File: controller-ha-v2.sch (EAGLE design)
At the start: 138 parts, among them U1 DS1307, U2 ARDUINO-MEGAPRO-5V, U3 ARDUINO-MEGAFULL

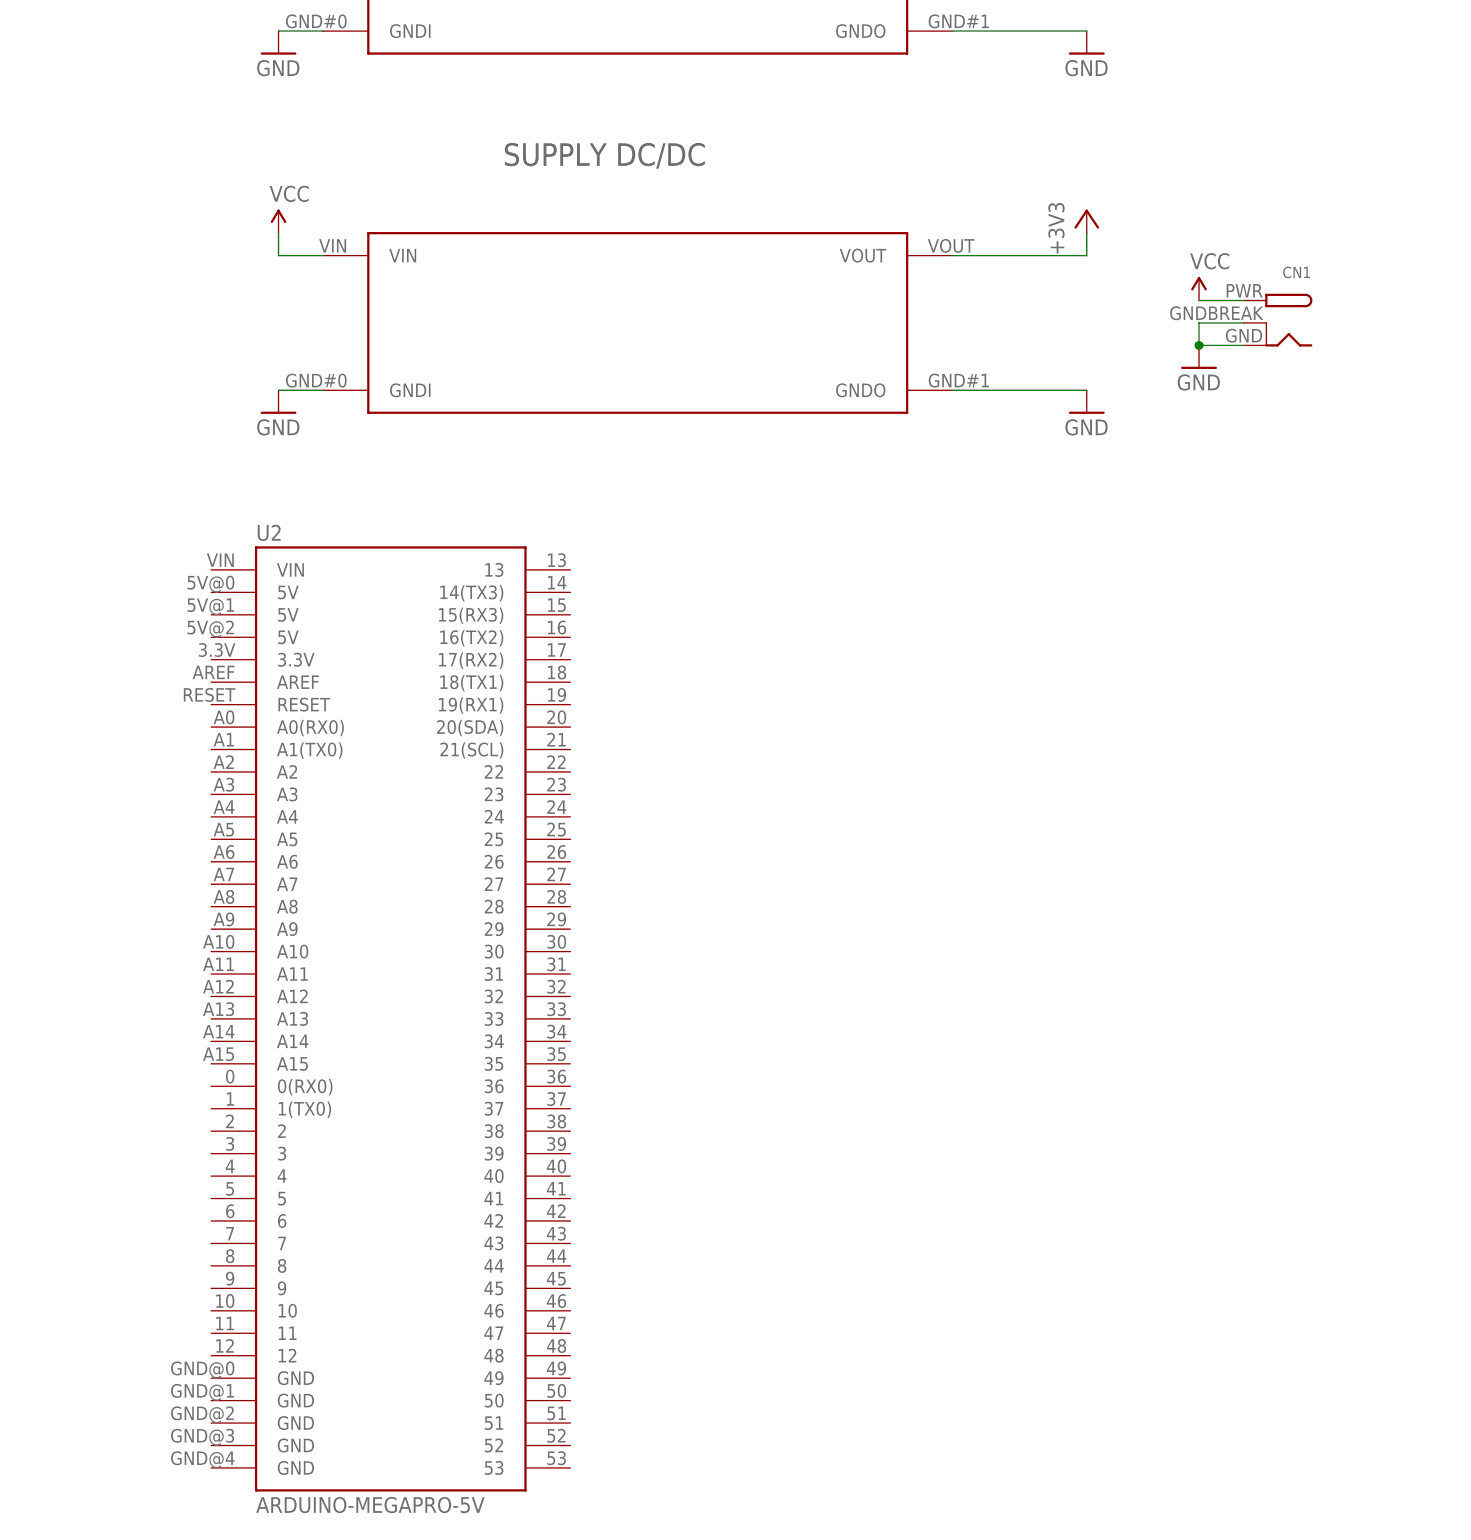
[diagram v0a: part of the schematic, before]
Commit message: Update to ver2
Added : Capacitors, DC/DC, DC input jack; Re-routed (fixed
too-close-through holes) + 9V DC and VCC clearence
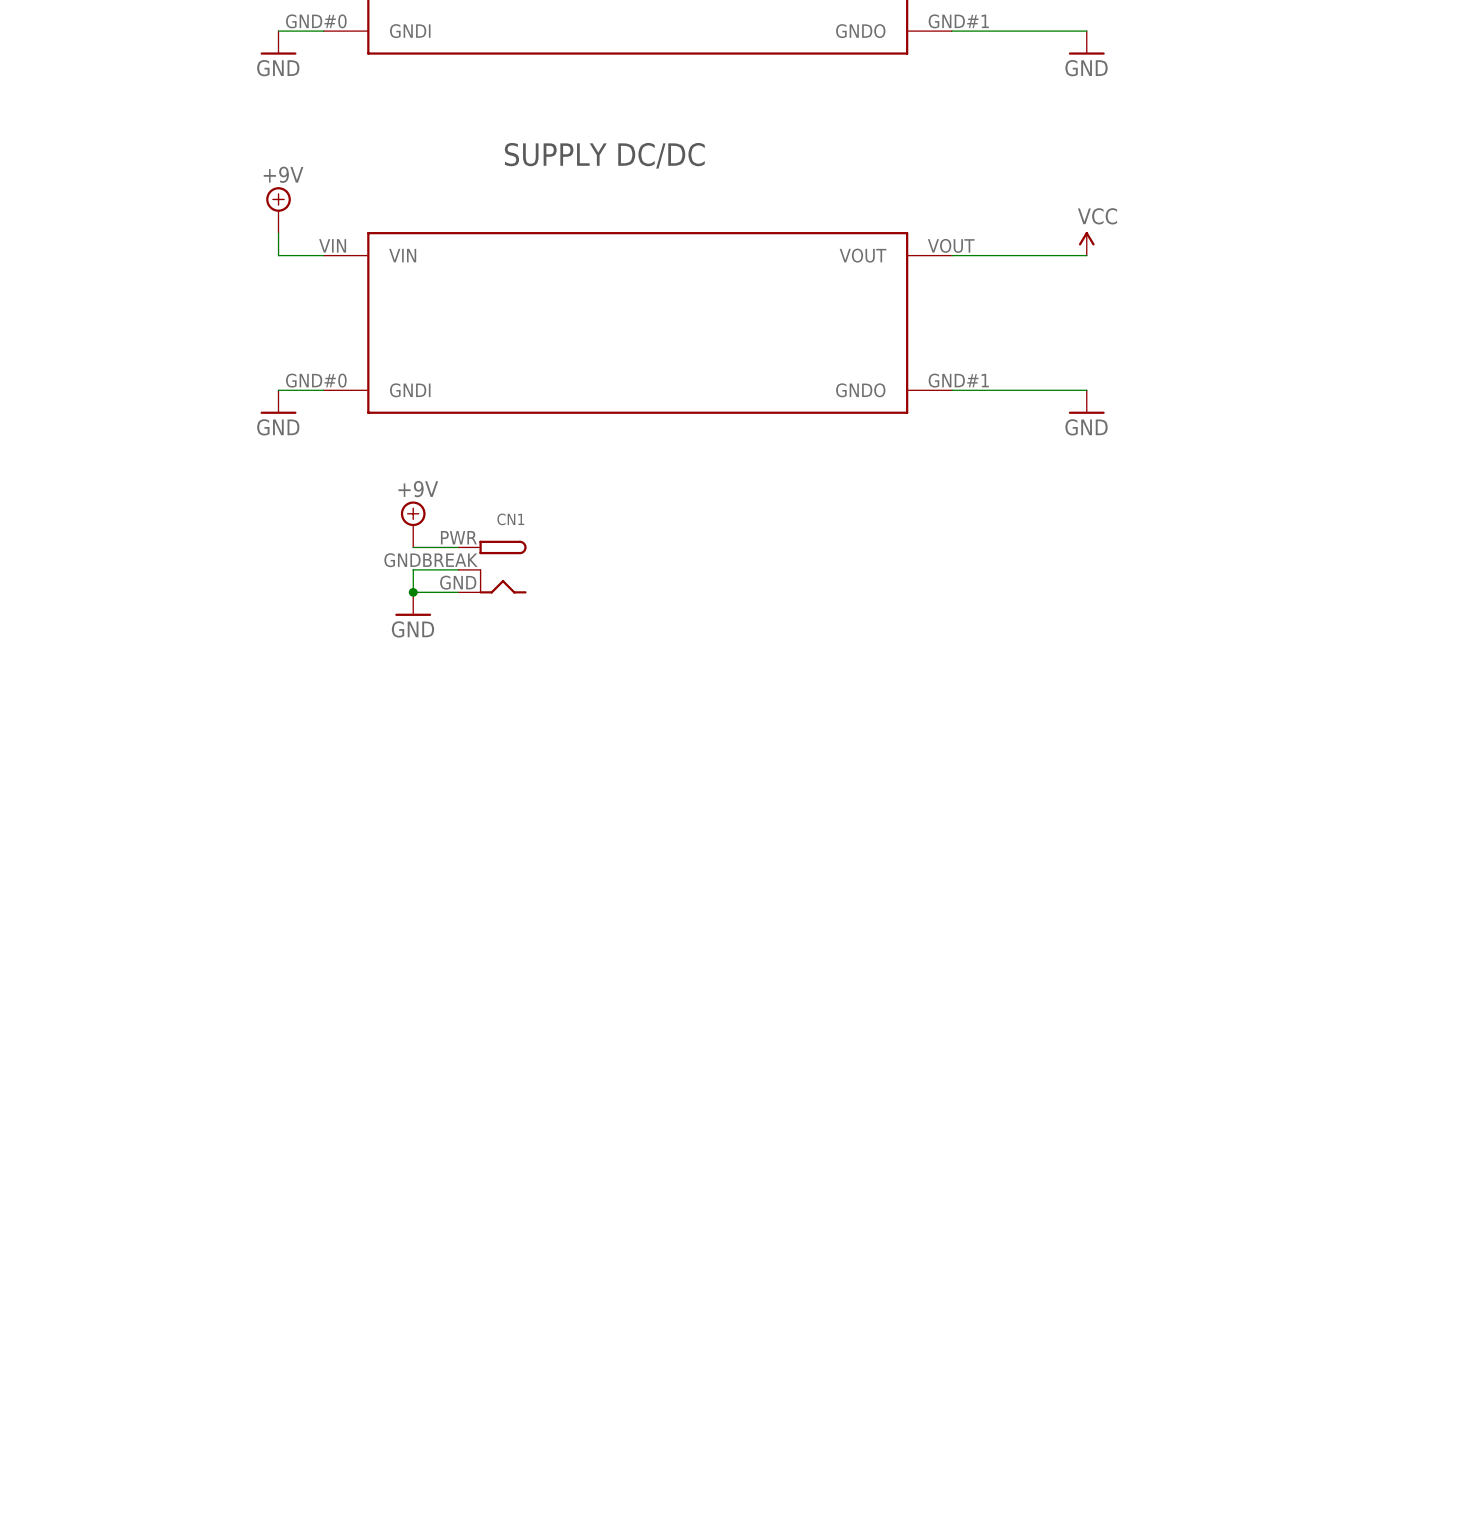
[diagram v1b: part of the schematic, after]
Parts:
- removed U2: ARDUINO-MEGAPRO-5V, SparkFun-Boards:ARDUINO-MEGAPRO-5V
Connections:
- new net +9V: CN1.PWR, U$1.VIN
- net +3V3: no longer U$1.VOUT
- net VCC: now also U$1.VOUT; no longer CN1.PWR, U$1.VIN
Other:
- moved on the sheet: CN1
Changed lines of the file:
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@@
 </class>
 <class number="1" name="power" width="0.3048" drill="0.6">
-<clearance class="1" value="0.254"/>
+<clearance class="1" value="0.8128"/>
 </class>
 <class number="2" name="GND" width="0.3048" drill="0.6">
@@
 <part name="U$1" library="bontor" deviceset="DCDCMODULE" device=""/>
 <part name="GND65" library="supply1" deviceset="GND" device=""/>
-<part name="+3V5" library="supply1" deviceset="+3V3" device=""/>
 <part name="GND66" library="supply1" deviceset="GND" device=""/>
-<part name="P+59" library="SparkFun" deviceset="VCC" device=""/>
 <part name="CN1" library="adafruit" deviceset="DCBARREL" device="PTH"/>
-<part name="P+60" library="SparkFun" deviceset="VCC" device=""/>
 <part name="GND67" library="supply1" deviceset="GND" device=""/>
 <part name="C9-100N1" library="rcl" deviceset="C-EU" device="C0603"/>
@@
 <part name="C9-100N25" library="rcl" deviceset="C-EU" device="C0603"/>
 <part name="C9-100N26" library="rcl" deviceset="C-EU" device="C0603"/>
-<part name="U2" library="SparkFun-Boards" deviceset="ARDUINO-MEGA" device="PRO-5V"/>
+<part name="P+61" library="SparkFun" deviceset="VCC" device=""/>
+<part name="SUPPLY1" library="supply2" deviceset="+9V" device=""/>
+<part name="SUPPLY3" library="supply2" deviceset="+9V" device=""/>
 </parts>
 <sheets>
@@
 <instance part="U$1" gate="G$1" x="497.84" y="114.3"/>
 <instance part="GND65" gate="1" x="548.64" y="104.14"/>
-<instance part="+3V5" gate="G$1" x="548.64" y="127"/>
 <instance part="GND66" gate="1" x="457.2" y="104.14"/>
-<instance part="P+59" gate="1" x="457.2" y="124.46"/>
-<instance part="CN1" gate="G$1" x="568.96" y="114.3" rot="MR0"/>
-<instance part="P+60" gate="1" x="561.34" y="116.84"/>
-<instance part="GND67" gate="1" x="561.34" y="109.22"/>
+<instance part="CN1" gate="G$1" x="480.06" y="86.36" rot="MR0"/>
+<instance part="GND67" gate="1" x="472.44" y="81.28"/>
 <instance part="C9-100N1" gate="G$1" x="20.32" y="215.9" rot="R270"/>
 <instance part="C9-100N2" gate="G$1" x="63.5" y="215.9" rot="R270"/>
@@
 <instance part="C9-100N25" gate="G$1" x="581.66" y="393.7" rot="R270"/>
 <instance part="C9-100N26" gate="G$1" x="632.46" y="393.7" rot="R270"/>
-<instance part="U2" gate="G$1" x="469.9" y="35.56"/>
+<instance part="P+61" gate="1" x="548.64" y="121.92"/>
+<instance part="SUPPLY1" gate="G$1" x="457.2" y="127"/>
+<instance part="SUPPLY3" gate="G$1" x="472.44" y="91.44"/>
 </instances>
 <busses>
@@
 <segment>
 <pinref part="CN1" gate="G$1" pin="GND"/>
-<wire x1="566.42" y1="111.76" x2="561.34" y2="111.76" width="0.1524" layer="91"/>
+<wire x1="477.52" y1="83.82" x2="472.44" y2="83.82" width="0.1524" layer="91"/>
 <pinref part="GND67" gate="1" pin="GND"/>
 <pinref part="CN1" gate="G$1" pin="GNDBREAK"/>
-<wire x1="566.42" y1="114.3" x2="561.34" y2="114.3" width="0.1524" layer="91"/>
-<wire x1="561.34" y1="114.3" x2="561.34" y2="111.76" width="0.1524" layer="91"/>
-<junction x="561.34" y="111.76"/>
+<wire x1="477.52" y1="86.36" x2="472.44" y2="86.36" width="0.1524" layer="91"/>
+<wire x1="472.44" y1="86.36" x2="472.44" y2="83.82" width="0.1524" layer="91"/>
+<junction x="472.44" y="83.82"/>
 </segment>
 </net>
@@
 <label x="302.26" y="167.64" size="1.778" layer="95"/>
 </segment>
-<segment>
-<pinref part="U$1" gate="G$1" pin="VOUT"/>
-<pinref part="+3V5" gate="G$1" pin="+3V3"/>
-<wire x1="533.4" y1="121.92" x2="548.64" y2="121.92" width="0.1524" layer="91"/>
-<wire x1="548.64" y1="121.92" x2="548.64" y2="124.46" width="0.1524" layer="91"/>
-</segment>
 </net>
 <net name="USIM_CLK" class="0">
@@
 </segment>
 </net>
-<net name="VCC" class="0">
+<net name="VCC" class="1">
 <segment>
 <pinref part="U1" gate="G$1" pin="VCC"/>
@@
 </segment>
 <segment>
-<pinref part="U$1" gate="G$1" pin="VIN"/>
-<wire x1="462.28" y1="121.92" x2="457.2" y2="121.92" width="0.1524" layer="91"/>
-<wire x1="457.2" y1="124.46" x2="457.2" y2="121.92" width="0.1524" layer="91"/>
-<pinref part="P+59" gate="1" pin="VCC"/>
-</segment>
-<segment>
-<pinref part="CN1" gate="G$1" pin="PWR"/>
-<wire x1="566.42" y1="116.84" x2="561.34" y2="116.84" width="0.1524" layer="91"/>
-<pinref part="P+60" gate="1" pin="VCC"/>
+<pinref part="U$1" gate="G$1" pin="VOUT"/>
+<wire x1="533.4" y1="121.92" x2="548.64" y2="121.92" width="0.1524" layer="91"/>
+<pinref part="P+61" gate="1" pin="VCC"/>
 </segment>
 </net>
@@
 </segment>
 </net>
+<net name="+9V" class="2">
+<segment>
+<pinref part="U$1" gate="G$1" pin="VIN"/>
+<wire x1="462.28" y1="121.92" x2="457.2" y2="121.92" width="0.1524" layer="91"/>
+<wire x1="457.2" y1="124.46" x2="457.2" y2="121.92" width="0.1524" layer="91"/>
+<pinref part="SUPPLY1" gate="G$1" pin="+9V"/>
+</segment>
+<segment>
+<pinref part="CN1" gate="G$1" pin="PWR"/>
+<wire x1="477.52" y1="88.9" x2="472.44" y2="88.9" width="0.1524" layer="91"/>
+<pinref part="SUPPLY3" gate="G$1" pin="+9V"/>
+</segment>
+</net>
